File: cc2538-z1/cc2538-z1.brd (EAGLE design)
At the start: 56.8 x 35.6 mm, 51 parts, among them U1 CC2538, U2 CC1120_RHM_32, X1 FA-128

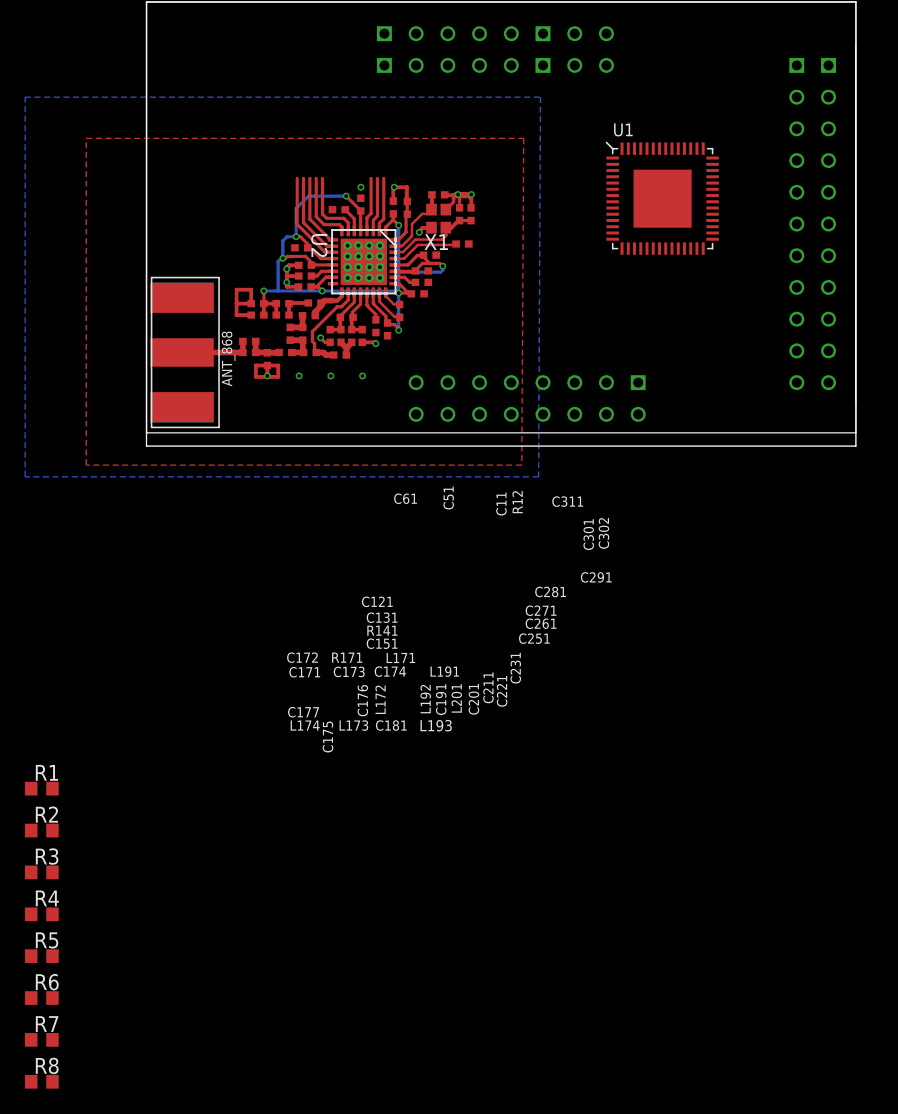
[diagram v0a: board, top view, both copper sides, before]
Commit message: Work on CC2538 board
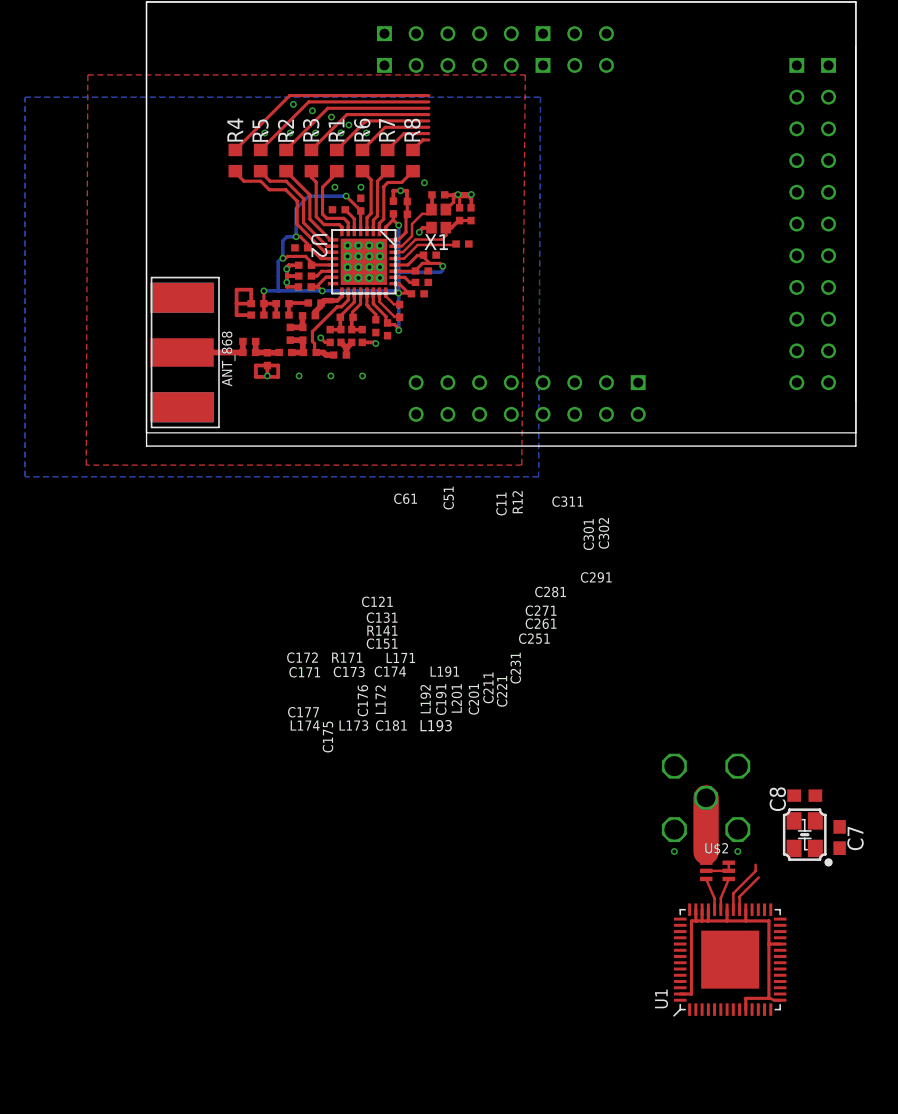
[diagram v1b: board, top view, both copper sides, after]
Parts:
- added C7, C8: 47p, rcl:C0603
- added U$1: SMATH, CC11x:SMA
- added U$2: BALUN-2.4G, CC11x:2450BM15A0015
- added X2: 32MHz, arm-cores:XTAL-3.2X2.5
- moved R8 79.5 mm to (21.3, 22.9), turned to 270 degrees
- moved R7 75.7 mm to (19.3, 22.9), turned to 270 degrees
- moved R6 71.8 mm to (17.3, 22.9), turned to 270 degrees
- moved R5 66.1 mm to (9.14, 22.9), turned to 270 degrees
- moved R4 62.3 mm to (7.12, 22.9), turned to 270 degrees
- moved U1 61.2 mm to (46.7, -41.1), turned to 90 degrees
- moved R3 60.9 mm to (13.2, 22.9), turned to 270 degrees
- moved R2 57.1 mm to (11.2, 22.9), turned to 270 degrees
- moved R1 55.6 mm to (15.2, 22.9), turned to 270 degrees
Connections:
- removed net N$70: U1.10
- new net +3V3: U1.10, U1.15, U1.24, U1.33, U1.36, U1.39, U1.40, U1.41, U1.55
- new net 2.4G: U$1.SIG, U$2.1
- new net 32M_Q1: C7.2, U1.34, X2.1
- new net 32M_Q2: C8.2, U1.35, X2.3
- new net N$28: U$2.4, U1.37
- new net N$29: U$2.3, U1.38
- net GND: now also C7.1, C8.1, U$1.GND1, U$1.GND2, U$1.GND3, U$1.GND4, U$2.2, U$2.5, U$2.6, U1.PAD, X2.2, X2.4
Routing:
- net +3V3: track 0.00 -> 28.2 mm
- net RADIO_SPI_CSN: track 7.48 -> 29.0 mm
- net RADIO_GPIO0: track 6.70 -> 24.5 mm
- net RADIO_SPI_MISO: track 6.12 -> 20.3 mm
- net RADIO_SPI_CLK: track 5.78 -> 17.1 mm
- net RADIO_SPI_MOSI: track 5.87 -> 15.2 mm
- net RADIO_GPIO2: track 4.35 -> 11.3 mm
- net 2.4G: track 0.00 -> 5.21 mm
- net RADIO_GPIO3: track 4.35 -> 9.11 mm
- net 32M_Q2: track 0.00 -> 4.34 mm
- net RADIO_RESET_N: track 4.36 -> 8.15 mm
- net 32M_Q1: track 0.00 -> 3.21 mm
- net N$29: track 0.00 -> 2.60 mm
- net N$28: track 0.00 -> 2.59 mm
- net GND: track 34.0 -> 35.8 mm, vias 13 -> 26

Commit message: CC2538 design work
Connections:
- net N$40 renamed ADC_1
- net N$41 renamed ADC_2
- net N$44 renamed DIGITAL_IO_2
- net N$46 renamed ADC_BATVOLTS
- net N$48 renamed DIGITAL_IO_1
- net N$51 renamed PWR_SENSE_EN
- net N$52 renamed PWR_RADIO_EN
- net N$55 renamed RS485_TXEN
- net N$57 renamed GPIO_INT_RAIN
- removed net N$53: H1.C42
- removed net N$58: H1.C48
- removed net N$59: H1.C43
- removed net N$62: H1.B22, H1.C40
- net +3V3: now also H1.B22, H1.C40
- net RADIO_GPIO3: now also H1.C42
- net RADIO_RESET_N: now also H1.C43
- net RADIO_SPI_CSN: now also H1.C48
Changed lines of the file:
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@@
 <wire x1="21.336" y1="23.71" x2="22.137" y2="24.511" width="0.254" layer="1"/>
 <wire x1="22.137" y1="24.511" x2="22.606" y2="24.511" width="0.254" layer="1"/>
+<contactref element="H1" pad="C43"/>
 <wire x1="21.336" y1="22.01" x2="21.336" y2="23.71" width="0" layer="19" extent="1-1"/>
-<wire x1="45.986" y1="-45.1226" x2="18.6436" y2="17.2212" width="0" layer="19" extent="1-1"/>
+<wire x1="34.29" y1="5.08" x2="18.6436" y2="17.2212" width="0" layer="19" extent="1-1"/>
+<wire x1="45.986" y1="-45.1226" x2="34.29" y2="5.08" width="0" layer="19" extent="1-1"/>
 </signal>
 <signal name="RADIO_GPIO3">
@@
 <wire x1="19.304" y1="23.71" x2="20.613" y2="25.019" width="0.254" layer="1"/>
 <wire x1="20.613" y1="25.019" x2="22.606" y2="25.019" width="0.254" layer="1"/>
+<contactref element="H1" pad="C42"/>
 <wire x1="19.304" y1="22.01" x2="19.304" y2="23.71" width="0" layer="19" extent="1-1"/>
+<wire x1="36.83" y1="2.54" x2="18.161" y2="17.2212" width="0" layer="19" extent="1-1"/>
 </signal>
 <signal name="RADIO_GPIO2">
@@
 <wire x1="7.1172" y1="23.7134" x2="11.4708" y2="28.067" width="0.254" layer="1"/>
 <wire x1="11.4708" y1="28.067" x2="22.606" y2="28.067" width="0.254" layer="1"/>
-<wire x1="7.1172" y1="22.0134" x2="7.1172" y2="23.7134" width="0" layer="19" extent="1-1"/>
-<wire x1="42.736" y1="-41.3726" x2="14.9352" y2="15.5194" width="0" layer="19" extent="1-1"/>
+<contactref element="H1" pad="C48"/>
+<wire x1="14.9352" y1="15.5194" x2="29.21" y2="2.54" width="0" layer="19" extent="1-1"/>
+<wire x1="7.1172" y1="23.7134" x2="7.1172" y2="22.0134" width="0" layer="19" extent="1-1"/>
+<wire x1="42.736" y1="-41.3726" x2="29.21" y2="2.54" width="0" layer="19" extent="1-1"/>
 </signal>
 <signal name="N$6">
@@
 <contactref element="H1" pad="A15"/>
 </signal>
-<signal name="N$40">
+<signal name="ADC_1">
 <contactref element="H1" pad="A16"/>
 </signal>
-<signal name="N$41">
+<signal name="ADC_2">
 <contactref element="H1" pad="A9"/>
 </signal>
@@
 <contactref element="H1" pad="A7"/>
 </signal>
-<signal name="N$44">
+<signal name="DIGITAL_IO_2">
 <contactref element="H1" pad="A10"/>
 </signal>
@@
 <contactref element="H1" pad="A8"/>
 </signal>
-<signal name="N$46">
+<signal name="ADC_BATVOLTS">
 <contactref element="H1" pad="A6"/>
 </signal>
@@
 <wire x1="19.05" y1="30.48" x2="19.05" y2="33.02" width="0" layer="19" extent="1-1"/>
 </signal>
-<signal name="N$48">
+<signal name="DIGITAL_IO_1">
 <contactref element="H1" pad="C51"/>
 </signal>
@@
 <contactref element="H1" pad="C50"/>
 </signal>
-<signal name="N$51">
+<signal name="PWR_SENSE_EN">
 <contactref element="H1" pad="B32"/>
 </signal>
-<signal name="N$52">
+<signal name="PWR_RADIO_EN">
 <contactref element="H1" pad="B30"/>
-</signal>
-<signal name="N$53">
-<contactref element="H1" pad="C42"/>
 </signal>
 <signal name="N$54">
 <contactref element="H1" pad="C54"/>
 </signal>
-<signal name="N$55">
+<signal name="RS485_TXEN">
 <contactref element="H1" pad="C46"/>
 </signal>
@@
 <contactref element="H1" pad="C45"/>
 </signal>
-<signal name="N$57">
+<signal name="GPIO_INT_RAIN">
 <contactref element="H1" pad="C49"/>
-</signal>
-<signal name="N$58">
-<contactref element="H1" pad="C48"/>
-</signal>
-<signal name="N$59">
-<contactref element="H1" pad="C43"/>
 </signal>
 <signal name="N$60">
@@
 <signal name="N$61">
 <contactref element="H1" pad="C47"/>
-</signal>
-<signal name="N$62">
-<contactref element="H1" pad="B22"/>
-<contactref element="H1" pad="C40"/>
-<wire x1="39.37" y1="2.54" x2="54.61" y2="25.4" width="0" layer="19" extent="1-1"/>
 </signal>
 <signal name="N$63">
@@
 <wire x1="43.6372" y1="-43.8726" x2="43.6372" y2="-38.0238" width="0.254" layer="1"/>
 <wire x1="43.6372" y1="-38.0238" x2="43.986" y2="-38.0238" width="0.254" layer="1"/>
+<contactref element="H1" pad="B22"/>
+<contactref element="H1" pad="C40"/>
+<wire x1="39.37" y1="2.54" x2="54.61" y2="25.4" width="0" layer="19" extent="1-1"/>
+<wire x1="43.986" y1="-37.1226" x2="39.37" y2="2.54" width="0" layer="19" extent="1-1"/>
 </signal>
 </signals>

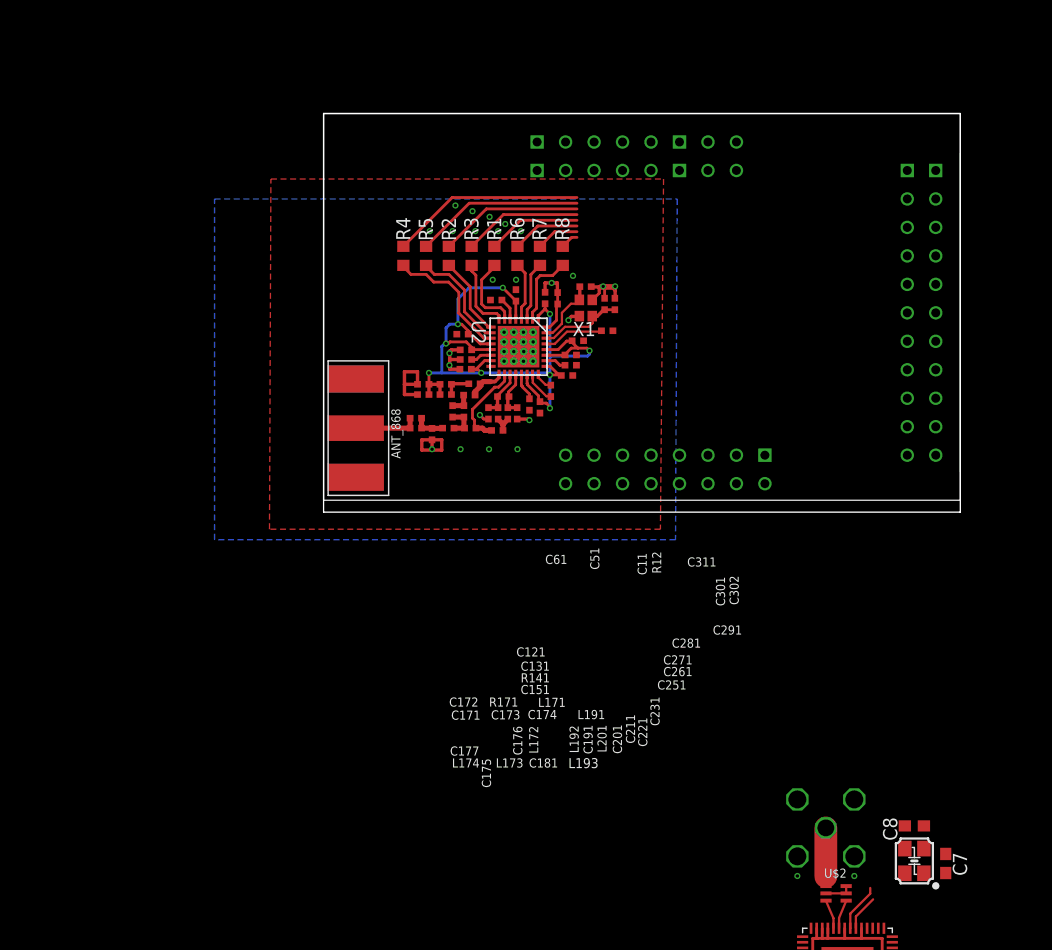
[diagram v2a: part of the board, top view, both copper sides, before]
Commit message: USB input layout done
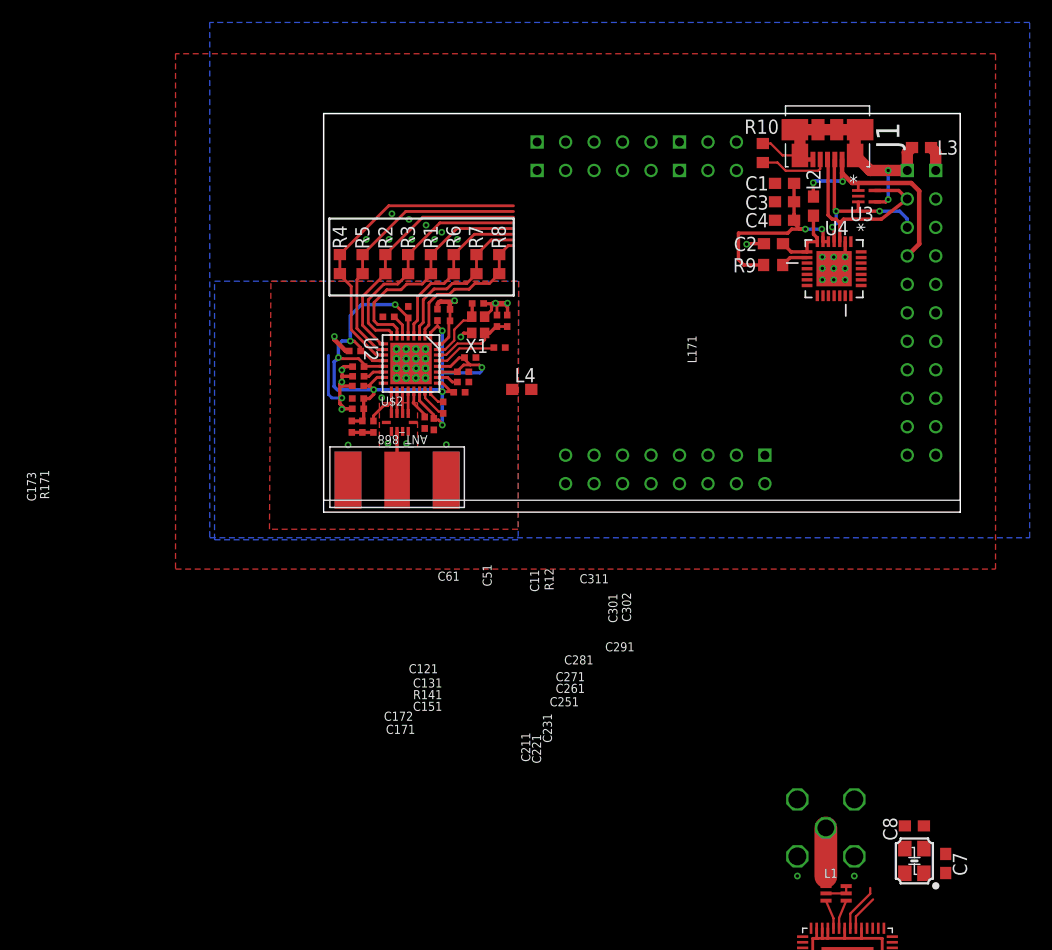
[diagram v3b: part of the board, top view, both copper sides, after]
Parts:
- removed C174, C175, C176, C177, C181, C191, C201, L172, L173, L174, L191, L192, L193, L201: (no value), CC11x:C0402_SMALL
- added C1: 4.7uF, CC11x:C0603
- added C2, C3: 1uF, CC11x:C0603
- added C4: 0.1uF, CC11x:C0603
- added J1: (no value), CC11x:MOLEX_47346-0001
- added L1: BALUN-2.4G, CC11x:2450BM15A0015
- added L2, L3, L4: BEAD, CC11x:C0603
- added R10: (no value), rcl:R0603
- added R9: 4.7k, rcl:R0603
- added U3: TPD2E001IDRLRQ1, Texas Instruments_By_element14_Batch_1:SOT50P160X60-5N
- added U4: CP2103, CC11x:QFN50P500X500X100-29N
- U$2: value BALUN-2.4G -> 0900PC15J0013; device CC11x:2450BM15A0015 -> CC11x:0900PC15J0013
- moved U$2 57.3 mm to (6.80, 8.00), turned to 0 degrees
- moved L171 9.81 mm to (4.45, 7.65), turned to 90 degrees
- moved C231 9.72 mm to (10.7, 9.30)
- moved C261 9.72 mm to (12.5, 11.6)
- moved C271 9.72 mm to (12.5, 12.5)
- moved C302 9.72 mm to (16.4, 17.1)
- moved U2 9.72 mm to (7.80, 13.3)
- moved C131 9.72 mm to (3.07, 13.0)
- moved C151 9.72 mm to (3.05, 11.3)
- moved C251 9.72 mm to (12.1, 10.7)
- moved C301 9.72 mm to (15.5, 17.1)
- moved C311 9.72 mm to (13.8, 18.6)
- moved C61 9.72 mm to (5.77, 17.4)
- moved R141 9.72 mm to (3.12, 12.1)
- moved X1 9.72 mm to (13.8, 16.7)
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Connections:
- net VDD renamed RVDD
- removed net 3: ANT_868.3
- removed net 4: ANT_868.4
- removed net N$34: H1.A13, H1.A3, H1.B23
- removed net N$35: H1.B19
- removed net N$36: H1.B21
- removed net N$37: H1.B17
- new net +3V3_SERIAL: C1.1, C3.1, C4.1, R9.2, U4.5, U4.6
- new net +5V: C2.2, L2.2, U4.7, U4.8
- new net +5V_USB: H1.A13, H1.A3, H1.B23, J1.1, L2.1, U3.1
- new net BSL_DTR: U4.27
- new net BSL_RTS: U4.23
- new net GNDA: H1.B17, J1.5, J1.M1, J1.M2, J1.M3, J1.M4, J1.M5, J1.M6, L3.1, R10.1, U3.4
- new net N$20: J1.4, R10.2
- new net N$26: U4.17
- new net N$27: R9.1, U4.9
- new net N$30: U4.16
- new net RGND: ANT_868.1, ANT_868.2, ANT_868.3, ANT_868.4, C11.2, C121.2, C131.2, C151.2, C171.2, C172.2, C211.2, C221.2, C251.2, C261.2, C271.2, C281.2, C291.2, C301.2, C302.2, C311.2, C51.2, C61.2, L4.1, R12.1, R12.2, R141.1, U$2.10, U$2.5, U$2.6, U$2.8, U$2.9, U2.32, U2.33, U2.V, U2.V_10, U2.V_11, U2.V_12, U2.V_13, U2.V_14, U2.V_15, U2.V_16, U2.V_2, U2.V_3, U2.V_4, U2.V_5, U2.V_6, U2.V_7, U2.V_8, U2.V_9, X1.2, X1.4
- new net USB_D_N: H1.B21, J1.2, U3.3, U4.4
- new net USB_D_P: H1.B19, J1.3, U3.5, U4.3
- net 2.4G: now also L1.1; no longer U$2.1
- net GND: now also C1.2, C2.1, C3.2, C4.2, L1.2, L1.5, L1.6, L3.2, L4.2, U4.2, U4.29; no longer ANT_868.1, ANT_868.2, C11.2, C121.2, C131.2, C151.2, C171.2, C172.2, C175.2, C201.2, C211.2, C221.2, C251.2, C261.2, C271.2, C281.2, C291.2, C301.2, C302.2, C311.2, C51.2, C61.2, L192.2, R12.1, R12.2, R141.1, U$2.2, U$2.5, U$2.6, U2.32, U2.33, U2.V, U2.V_10, U2.V_11, U2.V_12, U2.V_13, U2.V_14, U2.V_15, U2.V_16, U2.V_2, U2.V_3, U2.V_4, U2.V_5, U2.V_6, U2.V_7, U2.V_8, U2.V_9, X1.2, X1.4
- net N$10: now also U$2.2; no longer C191.1, L191.2, L192.1
- net N$11: now also ANT_868.RF, U$2.7; no longer C191.2, L193.1, L201.2
- net N$12: now also U$2.3; no longer C181.1, L193.2
- net N$14: now also U$2.4; no longer C174.1
- net N$15: now also U4.19; no longer C174.2, C176.1, L172.1
- net N$16: now also U4.26; no longer C176.2, C181.2, L172.2, L173.1
- net N$17: now also U4.18; no longer C175.1, C177.1, L173.2, L174.1
- net N$18: now also U4.22; no longer ANT_868.RF, C177.2, L174.2
- net N$28: now also L1.4; no longer U$2.4
- net N$29: now also L1.3; no longer U$2.3
- net N$9: now also U$2.1; no longer C201.1, L191.1, L201.1
- net UART0_RX: now also U4.25
- net UART0_TX: now also U4.24
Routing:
- net RGND: track 0.00 -> 30.1 mm, vias 0 -> 14
- net GNDA: track 0.00 -> 27.2 mm, vias 0 -> 2
- net +5V_USB: track 0.00 -> 20.5 mm, vias 0 -> 2
- net +3V3_SERIAL: track 0.00 -> 19.5 mm, vias 0 -> 2
- net USB_D_P: track 0.00 -> 18.0 mm
- net GND: track 35.8 -> 18.8 mm, vias 26 -> 21
- net USB_D_N: track 0.00 -> 15.9 mm, vias 0 -> 3
- net +5V: track 0.00 -> 6.74 mm
- net N$20: track 0.00 -> 6.33 mm
- net N$12: track 7.85 -> 2.00 mm
- net N$18: track 5.76 -> 0.00 mm
- net RADIO_SPI_MOSI: track 15.2 -> 20.9 mm
- net RADIO_RESET_N: track 8.15 -> 13.7 mm
- net RADIO_GPIO3: track 9.11 -> 14.6 mm
- net RADIO_SPI_CLK: track 17.1 -> 21.6 mm
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- added copper zone on layer 1, net RGND
- added copper zone on layer 16, net RGND

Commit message: Added Radio power filtering & switch.
I need to stop committing at 6am...
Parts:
- added C5, C6: 100nf, CC11x:C0603
- added F2: BALUN-2.4G, CC11x:2450BM15A0015
- added Q2: DMG6602SVT, farnell-parts:TSOT26
- added R11, R13: 100K, resistor:R0805
- L1: value BALUN-2.4G -> BEAD; device CC11x:2450BM15A0015 -> CC11x:C0603
- moved L1 51.0 mm to (17.6, 8.53), turned to 180 degrees
- moved L4 5.39 mm to (17.6, 5.56)
- renumbered U$2 to F1
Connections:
- new net N$31: C6.1, L1.1, Q2.P$4
- new net N$34: Q2.P$3, Q2.P$6, R11.1
- net +3V3: now also Q2.P$2, R11.2
- net 2.4G: now also F2.1; no longer L1.1
- net GND: now also C6.2, F2.2, F2.5, F2.6, Q2.P$5, R13.1; no longer L1.2, L1.5, L1.6
- net N$28: now also F2.4; no longer L1.4
- net N$29: now also F2.3; no longer L1.3
- net PWR_RADIO_EN: now also Q2.P$1, R13.2
- net RGND: now also C5.2
- net RVDD: now also C5.1, L1.2
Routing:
- net N$34: track 0.00 -> 18.1 mm
- net +3V3: track 28.2 -> 34.6 mm
- net RVDD: track 69.5 -> 75.8 mm
- net N$31: track 0.00 -> 3.46 mm
- net PWR_RADIO_EN: track 0.00 -> 2.33 mm, vias 0 -> 1
- net RGND: vias 14 -> 18
- net GND: vias 21 -> 26
